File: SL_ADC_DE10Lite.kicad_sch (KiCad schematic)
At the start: 24 parts, among them J1 DE10Lite header, J2 Conn_02x14_Odd_Even, J3 Conn_02x04_Odd_Even

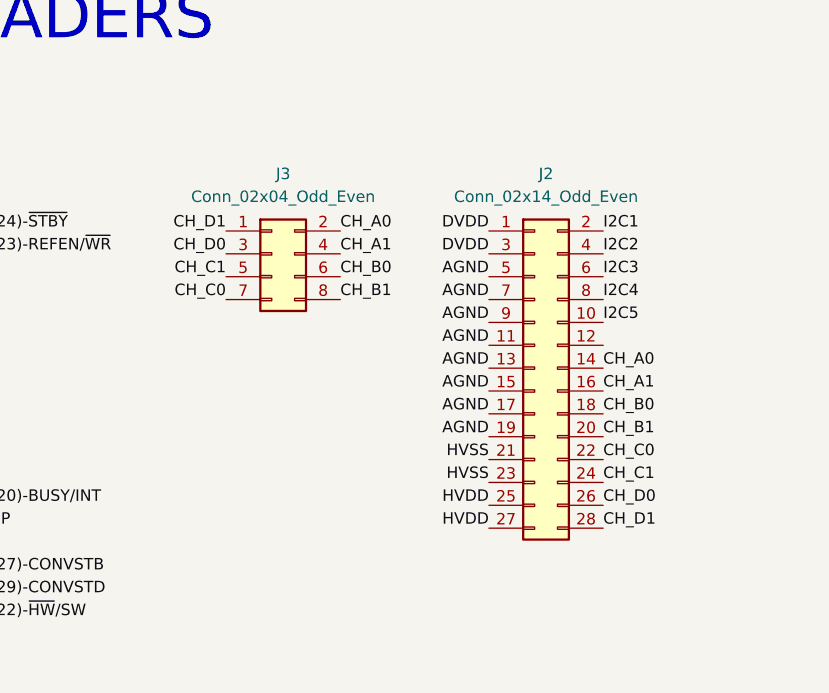
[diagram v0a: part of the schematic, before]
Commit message: Rounded corners!!!
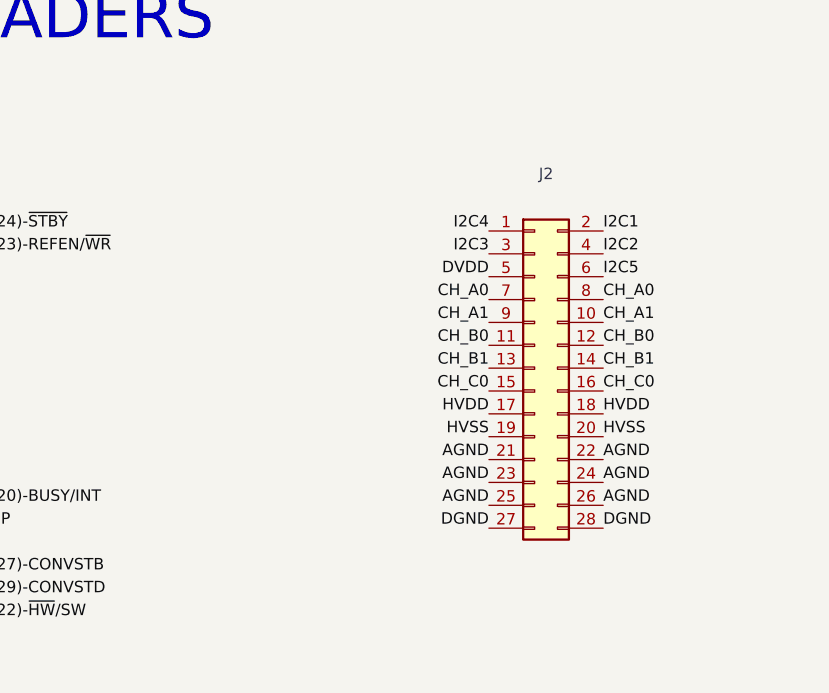
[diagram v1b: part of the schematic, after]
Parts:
- removed J3: Conn_02x04_Odd_Even, Connector_PinHeader_2.54mm:PinHeader_2x04_P2.54mm_Horizontal, symbol Connector_Generic:Conn_02x04_Odd_Even
- J2: value Conn_02x14_Odd_Even -> Analog header
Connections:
- net AGND: now also J2.21 (Pin_21), J2.22 (Pin_22), J2.23 (Pin_23), J2.24 (Pin_24), J2.25 (Pin_25), J2.26 (Pin_26); no longer J2.11 (Pin_11), J2.13 (Pin_13), J2.15 (Pin_15), J2.17 (Pin_17), J2.19 (Pin_19), J2.5 (Pin_5), J2.7 (Pin_7), J2.9 (Pin_9)
- net CH_A0: now also J2.7 (Pin_7), J2.8 (Pin_8); no longer J2.14 (Pin_14)
- net CH_A1: now also J2.10 (Pin_10), J2.9 (Pin_9); no longer J2.16 (Pin_16)
- net CH_B0: now also J2.11 (Pin_11), J2.12 (Pin_12); no longer J2.18 (Pin_18)
- net CH_B1: now also J2.13 (Pin_13), J2.14 (Pin_14); no longer J2.20 (Pin_20)
- net CH_C0: now also J2.15 (Pin_15), J2.16 (Pin_16); no longer J2.22 (Pin_22)
- net CH_C1: no longer J2.24 (Pin_24)
- net CH_D0: no longer J2.26 (Pin_26)
- net CH_D1: no longer J2.28 (Pin_28)
- net DGND: now also J2.27 (Pin_27), J2.28 (Pin_28)
- net DVDD: now also J2.5 (Pin_5); no longer J2.1 (Pin_1), J2.3 (Pin_3)
- net HVDD: now also J2.17 (Pin_17), J2.18 (Pin_18); no longer J2.25 (Pin_25), J2.27 (Pin_27)
- net HVSS: now also J2.19 (Pin_19), J2.20 (Pin_20); no longer J2.21 (Pin_21), J2.23 (Pin_23)
- net I2C3: now also J2.3 (Pin_3); no longer J2.6 (Pin_6)
- net I2C4: now also J2.1 (Pin_1); no longer J2.8 (Pin_8)
- net I2C5: now also J2.6 (Pin_6); no longer J2.10 (Pin_10)
